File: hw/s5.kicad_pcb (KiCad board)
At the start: 2 copper layers, 110 x 53 mm, 220 parts, among them J1 Conn_01x02, J12 USB_C_Receptacle, J2 RJ45, J3 RJ45, J4 RJ45, J5 RJ45, J6 RJ45, J7 Conn_01x03, Q1 NMOS, Q2 NMOS, Q3 NMOS, Q4 NMOS, Q5 NMOS, SW1 SW_Push, SW2 SW_Push, T1 GBE_XFMR, T2 GBE_XFMR, T3 GBE_XFMR, T4 GBE_XFMR, T5 GBE_XFMR, U1 KSZ9477S, U10 TPS3823, U11 TLV62569, U12 AP2112K-1.8, U13 TPS23861, U2 AMS1117-3.3, U3 AP2112K-2.5, U4 AP2112K-1.2, U6 TPS54560, U7 T113-S3, U8 W25Q128JVSIQ, U9 TPS23861, Y1 25MHz, Y2 24MHz, Y3 32.768kHz

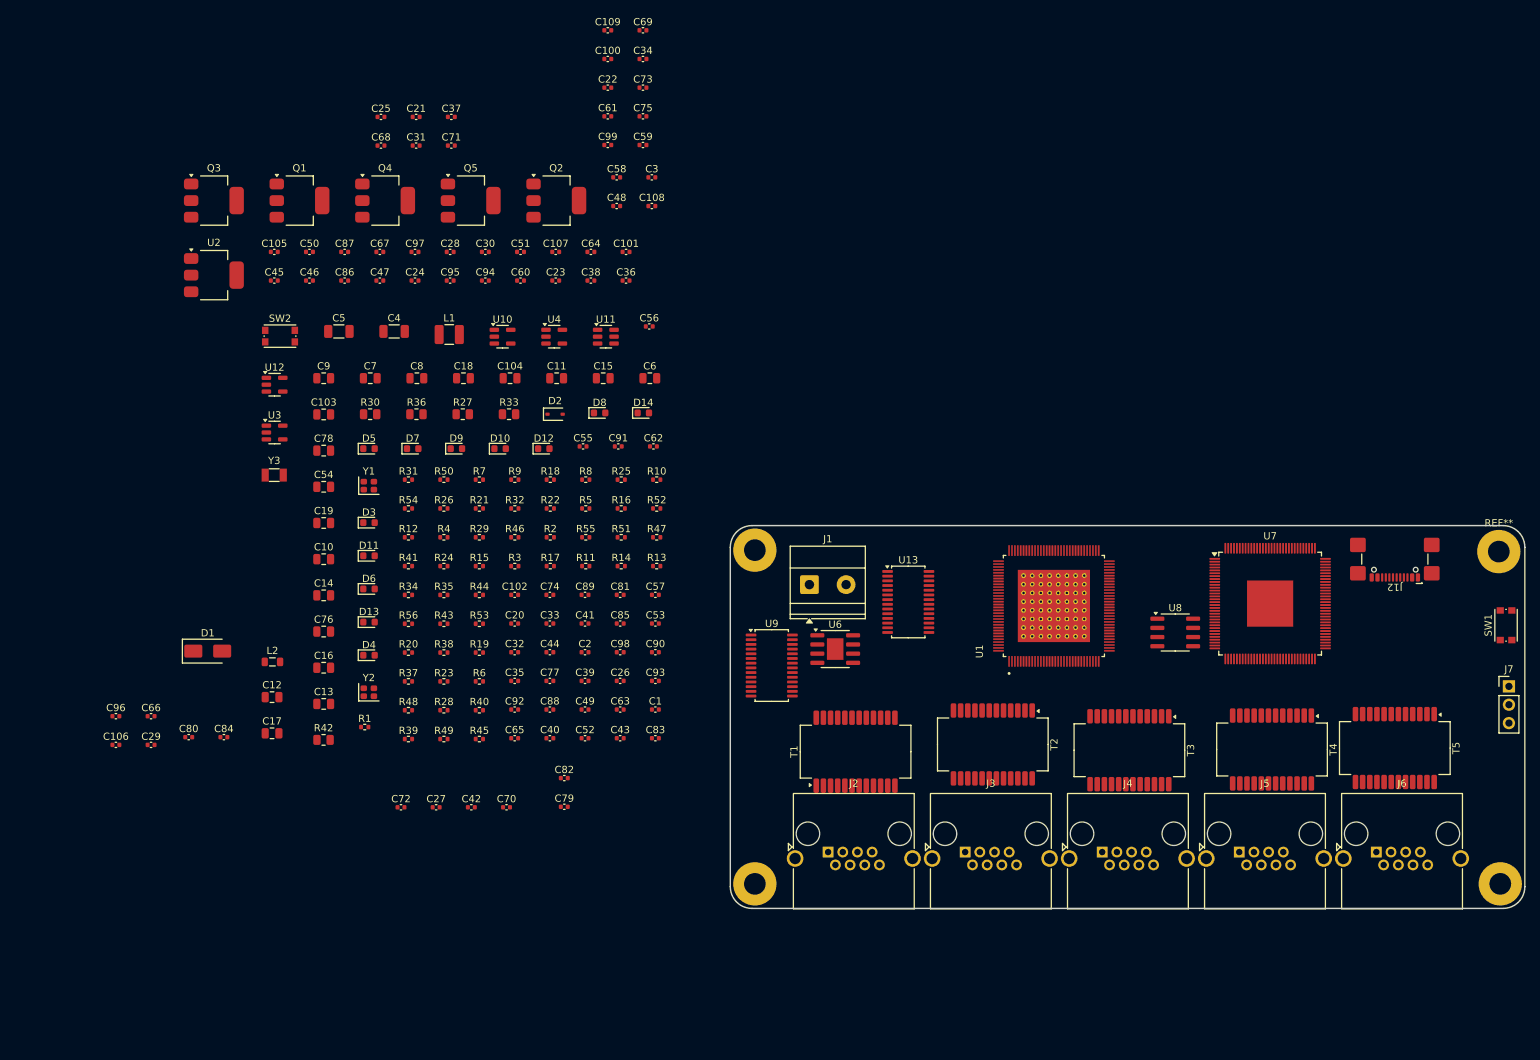
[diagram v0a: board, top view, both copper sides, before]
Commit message: Barrel jack, drop BOOT button, 256MB NAND flash, net classes
- Power input: terminal block -> 5.5/2.5mm barrel jack (48V Meanwell)
- Remove SW1 (FEL/boot button), keep only reset (SW2)
- Flash: W25Q128 SPI NOR (16MB) -> W25N02 SPI NAND (256MB) for
  full einheit stack + web UI
- Net classes: MDI (0.12mm/0.15mm clearance), RGMII, POWER with
  auto-assignment patterns; via sizes 0.3/0.45/0.6/0.8mm
- Track widths reduced to 0.12mm for KSZ9477 QFP escape (0.4mm pitch)
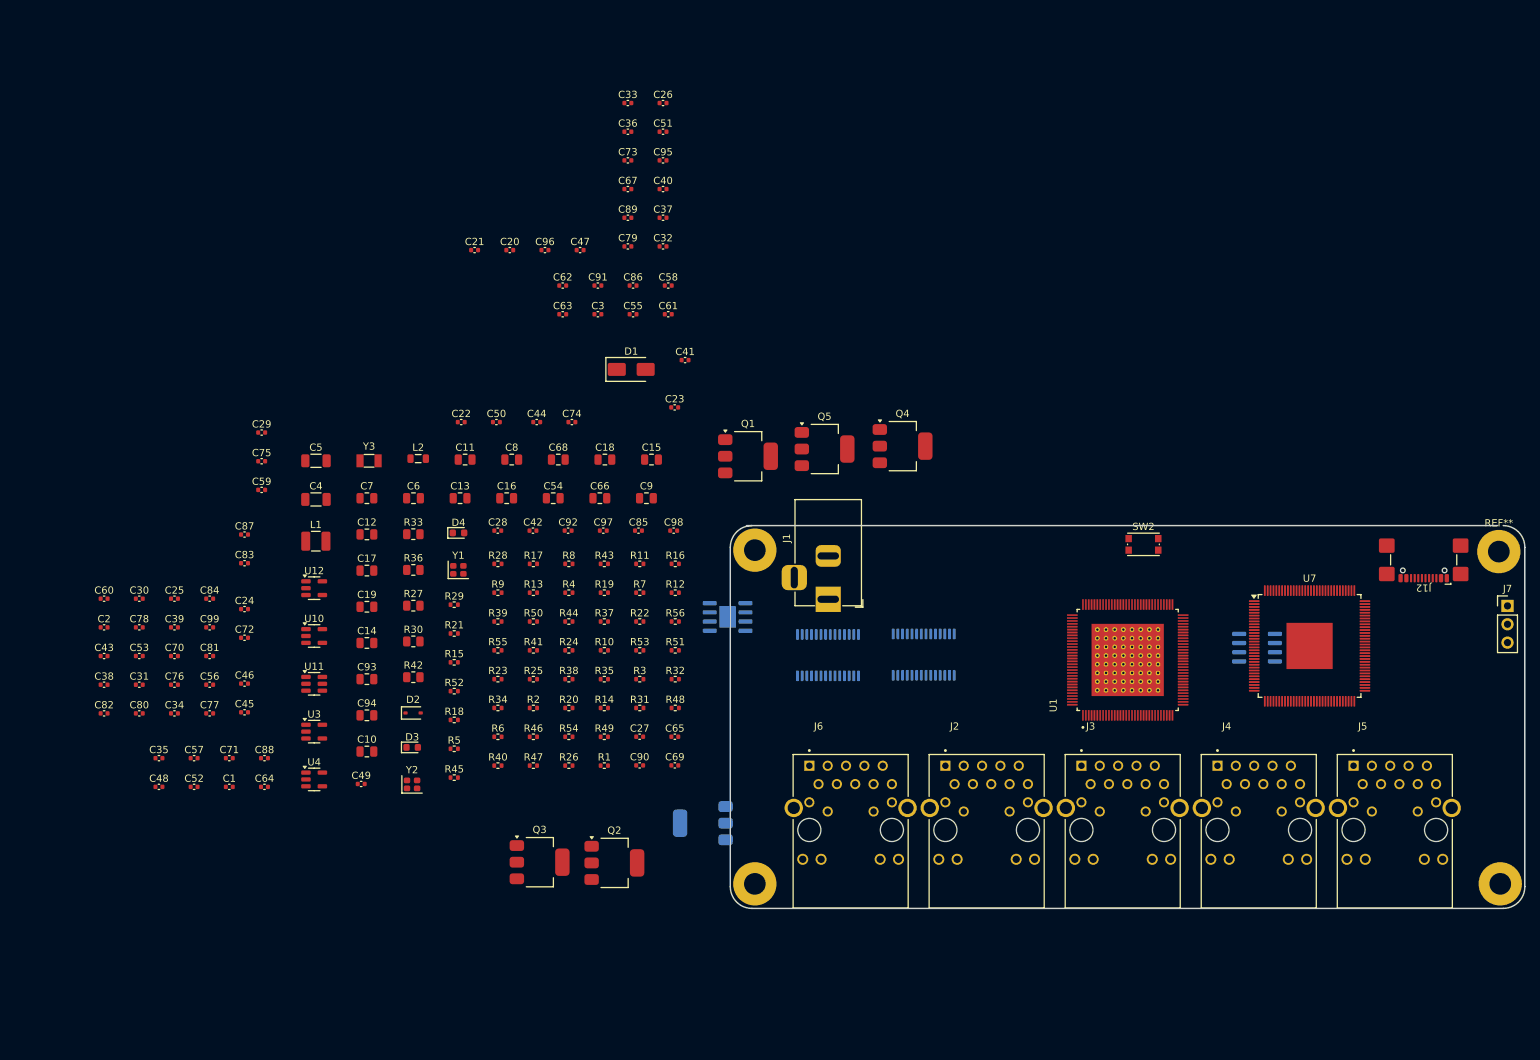
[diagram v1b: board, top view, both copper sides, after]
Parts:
- removed C100, C101, C102, C107, C108, C109: 100nF, Capacitor_SMD:C_0402_1005Metric
- removed C103, C104: 10uF, Capacitor_SMD:C_0805_2012Metric
- removed C105, C106: 18pF, Capacitor_SMD:C_0402_1005Metric
- removed D10, D11, D12, D13, D14, D5, D6, D7, D8, D9: LED, LED_SMD:LED_0603_1608Metric
- removed SW1: SW_Push, Button_Switch_SMD:SW_Push_1P1T_NO_CK_KMR2
- removed T1, T2, T3, T4, T5: GBE_XFMR, Transformer_SMD:Transformer_Ethernet_YDS_30F-51NL_SO-24_7.1x15.1mm
- C66, C68: footprint Capacitor_SMD:C_0402_1005Metric -> Capacitor_SMD:C_0805_2012Metric
- C69, C70: value 100nF -> 1uF
- C76, C78: footprint Capacitor_SMD:C_0805_2012Metric -> Capacitor_SMD:C_0402_1005Metric
- C79, C80: value 1uF -> 100nF
- C93, C94: value 100nF -> 10uF; footprint Capacitor_SMD:C_0402_1005Metric -> Capacitor_SMD:C_0805_2012Metric
- C95, C96: value 100nF -> 18pF
- J1: value Conn_01x02 -> BarrelJack; footprint TerminalBlock_Phoenix:TerminalBlock_Phoenix_MKDS-1,5-2-5.08_1x02_P5.08mm_Horizontal -> Connector_BarrelJack:BarrelJack_Horizontal
- J2, J3, J4, J5, J6: value RJ45 -> LPJG0926HENL; footprint Connector_RJ:RJ45_Amphenol_RJHSE5380 -> connectors:LPJG0926HENL
- R15, R16, R17, R18, R19, R20, R21, R22, R23, R24: value 270 -> 150
- U13, U2, U6, U8, U9: moved to B.Cu
- moved SW2 123.0 mm to (162.2, 87.6)
- moved C34 111.4 mm to (28.1, 111.0)
- moved C48 102.4 mm to (25.9, 121.2)
- moved Q3 102.1 mm to (78.6, 131.6)
- moved C69 101.9 mm to (97.3, 118.2)
- moved U2 101.7 mm to (101.2, 126.2), turned to 180 degrees
- moved Q2 92.0 mm to (89.0, 131.7)
- moved C71 90.2 mm to (35.6, 117.2)
- moved C96 87.7 mm to (79.3, 46.9)
- moved C38 87.6 mm to (18.3, 107.0)
- moved C64 86.8 mm to (40.5, 121.2)
- moved C99 86.6 mm to (32.9, 99.1)
- moved C31 83.9 mm to (23.2, 107.0)
- moved C26 80.2 mm to (95.7, 26.5)
- moved Q4 79.3 mm to (128.8, 74.0)
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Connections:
- C55 pad 1: P1_A_CT -> P1_CT1
- C56 pad 1: P1_B_CT -> P1_CT2
- C57 pad 1: P1_C_CT -> P2_CT1
- C58 pad 1: P1_D_CT -> P2_CT2
- C59 pad 1: P2_A_CT -> P3_CT1
- C60 pad 1: P2_B_CT -> P3_CT2
- C61 pad 1: P2_C_CT -> P4_CT1
- C62 pad 1: P2_D_CT -> P4_CT2
- C63 pad 1: P3_A_CT -> P5_CT1
- C64 pad 1: P3_B_CT -> P5_CT2
- C65 pad 1: P3_C_CT -> VDD_3V3
- C66 pad 1: P3_D_CT -> VIN_48V
- C67 pad 1: P4_A_CT -> VDD_3V3
- C68 pad 1: P4_B_CT -> VIN_48V
- C69 pad 1: P4_C_CT -> N$11
- C70 pad 1: P4_D_CT -> N$12
- C71 pad 1: P5_A_CT -> VDD_3V3
- C72 pad 1: P5_B_CT -> VDD_3V3
- C73 pad 1: P5_C_CT -> VDD_3V3
- C74 pad 1: P5_D_CT -> VDD_3V3
- C76 pad 1: VIN_48V -> VDD_3V3
- C78 pad 1: VIN_48V -> VDD_3V3
- C79 pad 1: N$1 -> VDD_3V3
- C80 pad 1: N$2 -> VDD_3V3
- C83 pad 1: VDD_3V3 -> VDD_CORE
- C84 pad 1: VDD_3V3 -> VDD_CORE
- C85 pad 1: VDD_3V3 -> VDD_CORE
- C86 pad 1: VDD_3V3 -> VDD_CORE
- C87 pad 1: VDD_3V3 -> VDD_CORE
- C88 pad 1: VDD_3V3 -> VDD_CORE
- C89 pad 1: VDD_3V3 -> VDD_1V8
- C90 pad 1: VDD_3V3 -> VDD_1V8
- C91 pad 1: VDD_3V3 -> VDD_1V8
- C92 pad 1: VDD_3V3 -> VDD_1V8
- C94 pad 1: VDD_CORE -> VDD_3V3
- C95 pad 1: VDD_CORE -> T113_DXIN
- C96 pad 1: VDD_CORE -> T113_DXOUT
- C97 pad 1: VDD_CORE -> SOC_RESET_N
- C98 pad 1: VDD_CORE -> VDD_3V3
- C99 pad 1: VDD_1V8 -> VDD_3V3
- D3 pad 1: ETH_LED1_0_A -> LED_PWR_A
- D3 pad 2: ETH_LED1_0 -> GND
- D4 pad 1: ETH_LED1_1_A -> LED_STA_A
- D4 pad 2: ETH_LED1_1 -> LED_STATUS
- J2 pad 1: P1_LINE_1 -> P1_AP
- J2 pad 2: P1_LINE_2 -> P1_AN
- J2 pad 3: P1_LINE_3 -> P1_BP
- J2 pad 4: P1_LINE_4 -> P1_CT1
- J2 pad 5: P1_LINE_5 -> P1_CT2
- J2 pad 6: P1_LINE_6 -> P1_BN
- J2 pad 7: P1_LINE_7 -> P1_CP
- J2 pad 8: P1_LINE_8 -> P1_CN
- J3 pad 1: P2_LINE_1 -> P2_AP
- J3 pad 2: P2_LINE_2 -> P2_AN
- J3 pad 3: P2_LINE_3 -> P2_BP
- J3 pad 4: P2_LINE_4 -> P2_CT1
- J3 pad 5: P2_LINE_5 -> P2_CT2
- J3 pad 6: P2_LINE_6 -> P2_BN
- J3 pad 7: P2_LINE_7 -> P2_CP
- J3 pad 8: P2_LINE_8 -> P2_CN
- J4 pad 1: P3_LINE_1 -> P3_AP
- J4 pad 2: P3_LINE_2 -> P3_AN
- J4 pad 3: P3_LINE_3 -> P3_BP
- J4 pad 4: P3_LINE_4 -> P3_CT1
- J4 pad 5: P3_LINE_5 -> P3_CT2
- J4 pad 6: P3_LINE_6 -> P3_BN
- J4 pad 7: P3_LINE_7 -> P3_CP
- J4 pad 8: P3_LINE_8 -> P3_CN
- J5 pad 1: P4_LINE_1 -> P4_AP
- J5 pad 2: P4_LINE_2 -> P4_AN
- J5 pad 3: P4_LINE_3 -> P4_BP
- J5 pad 4: P4_LINE_4 -> P4_CT1
- J5 pad 5: P4_LINE_5 -> P4_CT2
- J5 pad 6: P4_LINE_6 -> P4_BN
- J5 pad 7: P4_LINE_7 -> P4_CP
- J5 pad 8: P4_LINE_8 -> P4_CN
- J6 pad 1: P5_LINE_1 -> P5_AP
- J6 pad 2: P5_LINE_2 -> P5_AN
- J6 pad 3: P5_LINE_3 -> P5_BP
- J6 pad 4: P5_LINE_4 -> P5_CT1
- J6 pad 5: P5_LINE_5 -> P5_CT2
- J6 pad 6: P5_LINE_6 -> P5_BN
- J6 pad 7: P5_LINE_7 -> P5_CP
- J6 pad 8: P5_LINE_8 -> P5_CN
- R15 pad 2: ETH_LED1_0_A -> N$1
- R16 pad 2: ETH_LED1_1_A -> N$2
- R17 pad 2: ETH_LED2_0_A -> N$3
- R18 pad 2: ETH_LED2_1_A -> N$4
- R19 pad 2: ETH_LED3_0_A -> N$5
- R20 pad 2: ETH_LED3_1_A -> N$6
- R21 pad 2: ETH_LED4_0_A -> N$7
- R22 pad 2: ETH_LED4_1_A -> N$8
- R23 pad 2: ETH_LED5_0_A -> N$9
- R24 pad 2: ETH_LED5_1_A -> N$10
- U1 pad 102: ETH_LED5_0 -> P5_GRN
- U1 pad 103: ETH_LED5_1 -> P5_YEL
- U1 pad 105: ETH_LED1_0 -> P1_GRN
- U1 pad 106: ETH_LED1_1 -> P1_YEL
- U1 pad 85: ETH_LED4_0 -> P4_GRN
- U1 pad 86: ETH_LED4_1 -> P4_YEL
- U1 pad 88: ETH_LED3_0 -> P3_GRN
- U1 pad 89: ETH_LED3_1 -> P3_YEL
- U1 pad 91: ETH_LED2_0 -> P2_GRN
- U1 pad 92: ETH_LED2_1 -> P2_YEL
- U7 pad 28: N$1 -> N$11
- U7 pad 30: N$2 -> N$12
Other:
- outline, holes or cut-outs redrawn

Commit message: Add S5 switch adapter with PoE control, fix USB-C footprint
Software:
- Scaffold einheit-cli switch adapter from s100, ported to s5
  namespace with KSZ9477 DSA + TPS23861 PoE I2C control.
- Commands: show interfaces/counters/vlans/mac-table/poe/system,
  set poe enable/disable/reset, set hostname/ip/dns/ntp/user,
  shell, ping, traceroute, reboot.
- poe.cc: TPS23861 I2C driver skeleton — U9 (0x20, ports 1-4),
  U13 (0x28, port 5). Register map TODOs for voltage/current
  scaling.
- Builds and runs on host (0 errors, PoE gracefully degrades
  when I2C bus unavailable).

Hardware:
- Fix USB-C footprint: remove overlapping pads (A1/B12, A4/B9,
  A9/B4, A12/B1 merged), local copy in connectors.pretty.
- Named all anonymous nets (N$2-N$13 -> proper signal names).
- Added empty.kicad_wks page template.
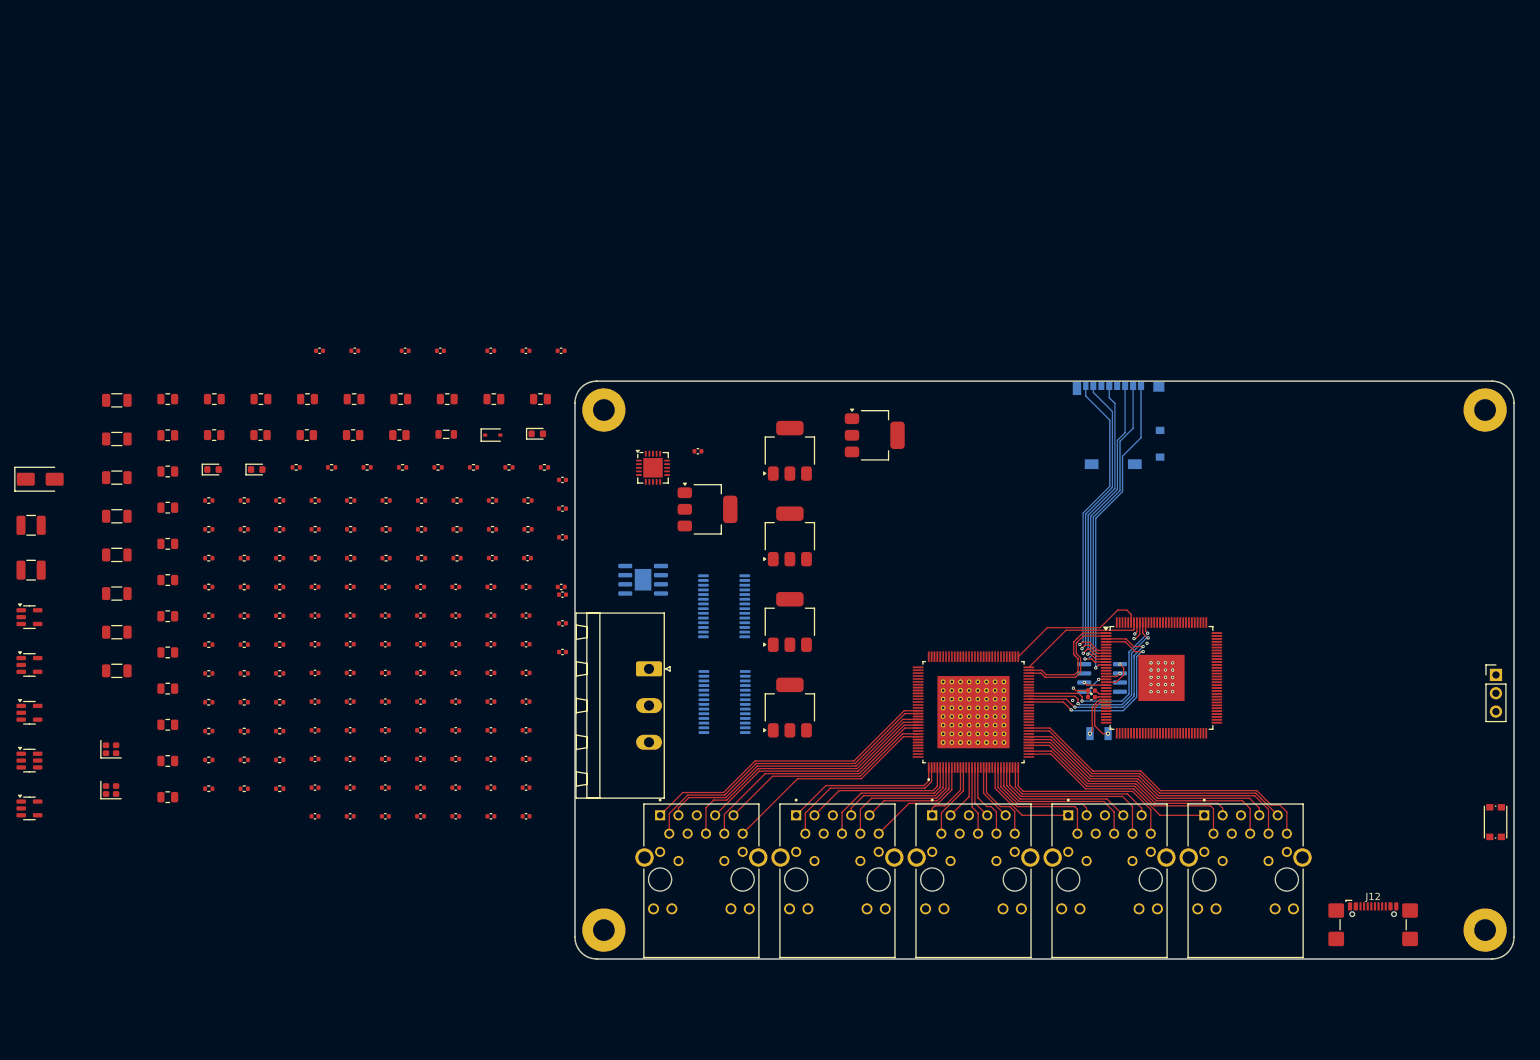
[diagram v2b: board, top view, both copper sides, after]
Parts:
- removed ? (x3): , 
- removed the REF** at (211.4, 88.6)
- added C100: 100nF, Capacitor_SMD:C_0402_1005Metric, F.Cu at (71.9, 113.3)
- added C101: 100nF, Capacitor_SMD:C_0402_1005Metric, F.Cu at (71.9, 109.4)
- added C102: 100nF, Capacitor_SMD:C_0402_1005Metric, F.Cu at (57.2, 105.4)
- added C103: 10uF, Capacitor_SMD:C_0805_2012Metric, F.Cu at (72.3, 67.5)
- added C104: 10uF, Capacitor_SMD:C_0805_2012Metric, F.Cu at (27.1, 107.6)
- added C105: 18pF, Capacitor_SMD:C_0402_1005Metric, F.Cu at (155.0, 108.8)
- added C106: 18pF, Capacitor_SMD:C_0402_1005Metric, F.Cu at (155.0, 107.8)
- added C107: 100nF, Capacitor_SMD:C_0402_1005Metric, F.Cu at (81.6, 60.8)
- added C108: 100nF, Capacitor_SMD:C_0402_1005Metric, F.Cu at (76.7, 109.4)
- added C109: 100nF, Capacitor_SMD:C_0402_1005Metric, F.Cu at (67.0, 117.3)
- added C110: 100nF, Capacitor_SMD:C_0402_1005Metric, F.Cu at (100.5, 74.7)
- added D5: LED, LED_SMD:LED_0603_1608Metric, F.Cu at (78.3, 72.3)
- added J8: microSD, Connector_Card:microSD_HC_Molex_104031-0811, B.Cu at (158.8, 71.1)
- added L3: 1uH, Inductor_SMD:L_0805_2012Metric, F.Cu at (65.7, 72.4)
- added R57: 10k, Resistor_SMD:R_0402_1005Metric, F.Cu at (37.7, 105.5)
- added R58: 10k, Resistor_SMD:R_0402_1005Metric, F.Cu at (44.9, 76.9)
- added R59: 27, Resistor_SMD:R_0402_1005Metric, F.Cu at (42.6, 97.5)
- added R60: 27, Resistor_SMD:R_0402_1005Metric, F.Cu at (72.1, 85.5)
- added R61: 5.1k, Resistor_SMD:R_0402_1005Metric, F.Cu at (32.8, 101.5)
- added R62: 5.1k, Resistor_SMD:R_0402_1005Metric, F.Cu at (77.0, 81.5)
- added R63: 270, Resistor_SMD:R_0402_1005Metric, F.Cu at (32.8, 113.5)
- added R64: 270, Resistor_SMD:R_0402_1005Metric, F.Cu at (42.6, 89.5)
- added R65: 270, Resistor_SMD:R_0402_1005Metric, F.Cu at (74.4, 76.9)
- added REF**: MountingHole_3mm_Pad, MountingHole:MountingHole_3mm_Pad, F.Cu at (209.5, 69.0)
- added REF**: MountingHole_3mm_Pad, MountingHole:MountingHole_3mm_Pad, F.Cu at (87.5, 141.0)
- added REF**: MountingHole_3mm_Pad, MountingHole:MountingHole_3mm_Pad, F.Cu at (209.5, 141.0)
- added REF**: MountingHole_3mm_Pad, MountingHole:MountingHole_3mm_Pad, F.Cu at (87.5, 69.0)
- added U14: LM5122, Package_DFN_QFN:QFN-20-1EP_4x4mm_P0.5mm_EP2.7x2.7mm, F.Cu at (94.3, 77.0)
- C1: value 100nF -> 100uF; footprint Capacitor_SMD:C_0402_1005Metric -> Capacitor_SMD:C_1206_3216Metric
- C10, C8, C9: footprint Capacitor_SMD:C_0805_2012Metric -> Capacitor_SMD:C_1206_3216Metric
- C11, C12, C54, C93, C94: value 10uF -> 100nF; footprint Capacitor_SMD:C_0805_2012Metric -> Capacitor_SMD:C_0402_1005Metric
- C13: value 10uF -> 15nF; footprint Capacitor_SMD:C_0805_2012Metric -> Capacitor_SMD:C_0402_1005Metric
- C14, C15: value 10uF -> 2.2uF; footprint Capacitor_SMD:C_0805_2012Metric -> Capacitor_SMD:C_1206_3216Metric
- C16, C17, C19: value 10uF -> 22uF
- C2: value 100nF -> 4.7uF; footprint Capacitor_SMD:C_0402_1005Metric -> Capacitor_SMD:C_0805_2012Metric
- C20: value 100nF -> 22uF; footprint Capacitor_SMD:C_0402_1005Metric -> Capacitor_SMD:C_0805_2012Metric
- C21, C22, C23, C24, C25, C26, C27, C28, C29, C64: value 100nF -> 10uF; footprint Capacitor_SMD:C_0402_1005Metric -> Capacitor_SMD:C_0805_2012Metric
- C3: value 15nF -> 100nF
- C4: value 2.2uF -> 100nF; footprint Capacitor_SMD:C_1206_3216Metric -> Capacitor_SMD:C_0402_1005Metric
- C5: value 2.2uF -> 10nF; footprint Capacitor_SMD:C_1206_3216Metric -> Capacitor_SMD:C_0402_1005Metric
- C52, C53: value 15pF -> 100nF
- C6, C7: value 22uF -> 10uF; footprint Capacitor_SMD:C_0805_2012Metric -> Capacitor_SMD:C_1206_3216Metric
- C62, C63: value 100nF -> 15pF
- C66, C68: footprint Capacitor_SMD:C_0805_2012Metric -> Capacitor_SMD:C_0402_1005Metric
- C69, C70: value 1uF -> 100nF
- C76, C78: footprint Capacitor_SMD:C_0402_1005Metric -> Capacitor_SMD:C_0805_2012Metric
- C79, C80: value 100nF -> 1uF
- C95, C96: value 18pF -> 100nF
- J1: value BarrelJack -> Conn_01x03; footprint Connector_BarrelJack:BarrelJack_Horizontal -> Connector_Phoenix_MSTB:PhoenixContact_MSTB_2,5_3-GF-5,08_1x03_P5.08mm_Horizontal_ThreadedFlange
- J12: footprint Connector_USB:USB_C_Receptacle_GCT_USB4110 -> connectors:USB_C_GCT_USB4110
- L1: value 33uH -> 10uH
- L2: value 1uH -> 33uH; footprint Inductor_SMD:L_0805_2012Metric -> Inductor_SMD:L_1210_3225Metric
- R1: value 24.9k -> 150k
- R10: value 4.7k -> 52.3k
- R12: value 10k -> 50k
- R13, R8: value 10k -> 100k
- R14: value 1k -> 6.04k
- R15: value 150 -> 191
- R16, R19, R20, R21: value 150 -> 10k
- R17, R18: value 150 -> 4.7k
- R2: value 52.3k -> 100k
- R22: value 150 -> 1k
- R25: value 10k -> 150
- R26, R29, R32: value 47 -> 150
- R27, R30: value 0.25 -> 150; footprint Resistor_SMD:R_0805_2012Metric -> Resistor_SMD:R_0402_1005Metric
- R28, R31: value 22 -> 150
- R3: value 10k -> 6.8k
- R33: value 0.25 -> 10k; footprint Resistor_SMD:R_0805_2012Metric -> Resistor_SMD:R_0402_1005Metric
- R34, R37, R43: value 22 -> 47
- R35, R41: value 47 -> 0.25; footprint Resistor_SMD:R_0402_1005Metric -> Resistor_SMD:R_0805_2012Metric
- R36, R42: value 0.25 -> 22; footprint Resistor_SMD:R_0805_2012Metric -> Resistor_SMD:R_0402_1005Metric
- R38, R44: value 22 -> 0.25; footprint Resistor_SMD:R_0402_1005Metric -> Resistor_SMD:R_0805_2012Metric
- R4: value 50k -> 33k
- R40, R49: value 10k -> 47
- R45, R46: value 4.7k -> 22
- R47: value 240 -> 22
- R5: value 100k -> 383k
- R50: value 10k -> 0.25; footprint Resistor_SMD:R_0402_1005Metric -> Resistor_SMD:R_0805_2012Metric
- R51, R52: value 27 -> 22
- R53, R54: value 5.1k -> 4.7k
- R55: value 270 -> 240
- R56: value 270 -> 10k
- R6: value 6.04k -> 10k
- R7: value 191 -> 10k
- R9: value 4.7k -> 24.9k
- U2: moved to F.Cu
- U8: value W25Q128JVSIQ -> W25N02JWZEIF
- Y3: moved to B.Cu
- moved C26 114.0 mm to (27.1, 117.6)
- moved Y3 107.9 mm to (156.1, 113.8)
- moved C33 95.8 mm to (76.7, 121.3)
- moved C21 86.8 mm to (27.1, 122.6)
- moved D1 83.2 mm to (9.46, 78.6)
- moved C55 79.8 mm to (52.4, 125.2)
- moved C40 77.3 mm to (76.7, 113.3)
- moved C79 76.5 mm to (62.1, 117.3)
- moved C91 76.3 mm to (47.5, 117.3)
- moved C36 76.2 mm to (76.7, 105.4)
- moved C51 74.9 mm to (71.9, 101.4)
- moved C95 74.9 mm to (71.9, 105.4)
- moved C15 74.4 mm to (20.1, 83.7)
- moved C23 74.1 mm to (27.1, 92.5)
- moved C9 73.7 mm to (20.1, 89.1)
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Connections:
- C1 pad 1: BOOT -> VIN_24V
- C1 pad 2: SW_NODE -> GND
- C10 pad 1: VDD_CORE -> VIN_24V
- C11 pad 1: VDD_1V8 -> BOOT
- C11 pad 2: GND -> SW_NODE
- C12 pad 1: VDD_1V8 -> SS_TR
- C13 pad 1: VIN_48V -> COMP_MID
- C14 pad 1: VDD_5V -> VIN_24V
- C15 pad 1: VDD_3V3 -> VIN_24V
- C16 pad 1: VDD_2V5 -> VDD_5V
- C17 pad 1: VDD_1V2 -> VDD_5V
- C18 pad 1: VDD_CORE -> VDD_5V
- C19 pad 1: VDD_1V8 -> VDD_CORE
- C2 pad 1: SS_TR -> BOOST_VCC
- C20 pad 1: VDD_2V5 -> VDD_CORE
- C21 pad 1: VDD_2V5 -> VDD_1V8
- C22 pad 1: VDD_2V5 -> VDD_1V8
- C23 pad 1: VDD_2V5 -> VIN_24V
- C24 pad 1: VDD_2V5 -> VDD_5V
- C25 pad 1: VDD_2V5 -> VDD_3V3
- C27 pad 1: VDD_2V5 -> VDD_1V2
- C28 pad 1: VDD_2V5 -> VDD_CORE
- C29 pad 1: VDD_1V2 -> VDD_1V8
- C3 pad 1: COMP_MID -> BST_BOOST
- C3 pad 2: GND -> BOOST_SW
- C30 pad 1: VDD_1V2 -> VDD_2V5
- C31 pad 1: VDD_1V2 -> VDD_2V5
- C32 pad 1: VDD_1V2 -> VDD_2V5
- C33 pad 1: VDD_1V2 -> VDD_2V5
- C34 pad 1: VDD_1V2 -> VDD_2V5
- C35 pad 1: VDD_1V2 -> VDD_2V5
- C36 pad 1: VDD_1V2 -> VDD_2V5
- C37 pad 1: VDD_1V2 -> VDD_2V5
- C38 pad 1: VDD_1V2 -> VDD_2V5
- C4 pad 1: VIN_48V -> BOOST_SS
- C49 pad 1: VDD_3V3 -> VDD_1V2
- C5 pad 1: VIN_48V -> BOOST_COMP_MID
- C50 pad 1: VDD_3V3 -> VDD_1V2
- C51 pad 1: VDD_3V3 -> VDD_1V2
- C52 pad 1: KSZ_XI -> VDD_1V2
- C53 pad 1: KSZ_XO -> VDD_1V2
- C54 pad 1: KSZ_RESET_N -> VDD_1V2
- C55 pad 1: P1_CT1 -> VDD_1V2
- C56 pad 1: P1_CT2 -> VDD_1V2
- C57 pad 1: P2_CT1 -> VDD_1V2
- C58 pad 1: P2_CT2 -> VDD_1V2
- C59 pad 1: P3_CT1 -> VDD_3V3
- C6 pad 1: VDD_5V -> VBUS_48V
- C60 pad 1: P3_CT2 -> VDD_3V3
- C61 pad 1: P4_CT1 -> VDD_3V3
- C62 pad 1: P4_CT2 -> KSZ_XI
- C63 pad 1: P5_CT1 -> KSZ_XO
- C64 pad 1: P5_CT2 -> KSZ_RESET_N
- C65 pad 1: VDD_3V3 -> P1_CT1
- C66 pad 1: VIN_48V -> P1_CT2
- C67 pad 1: VDD_3V3 -> P2_CT1
- C68 pad 1: VIN_48V -> P2_CT2
- C69 pad 1: N$11 -> P3_CT1
- C7 pad 1: VDD_5V -> VBUS_48V
- C70 pad 1: N$12 -> P3_CT2
- C71 pad 1: VDD_3V3 -> P4_CT1
- C72 pad 1: VDD_3V3 -> P4_CT2
- C73 pad 1: VDD_3V3 -> P5_CT1
- C74 pad 1: VDD_3V3 -> P5_CT2
- C76 pad 1: VDD_3V3 -> VBUS_48V
- C78 pad 1: VDD_3V3 -> VBUS_48V
- C79 pad 1: VDD_3V3 -> N$12
- C8 pad 1: VDD_5V -> VBUS_48V
- C80 pad 1: VDD_3V3 -> N$13
- C83 pad 1: VDD_CORE -> VDD_3V3
- C84 pad 1: VDD_CORE -> VDD_3V3
- C85 pad 1: VDD_CORE -> VDD_3V3
- C86 pad 1: VDD_CORE -> VDD_3V3
- C87 pad 1: VDD_CORE -> VDD_3V3
- C88 pad 1: VDD_CORE -> VDD_3V3
- C89 pad 1: VDD_1V8 -> VDD_3V3
- C9 pad 1: VDD_CORE -> VIN_24V
- C90 pad 1: VDD_1V8 -> VDD_3V3
- C91 pad 1: VDD_1V8 -> VDD_3V3
- C92 pad 1: VDD_1V8 -> VDD_3V3
- C94 pad 1: VDD_3V3 -> VDD_CORE
- C95 pad 1: T113_DXIN -> VDD_CORE
- C96 pad 1: T113_DXOUT -> VDD_CORE
- C97 pad 1: SOC_RESET_N -> VDD_CORE
- C98 pad 1: VDD_3V3 -> VDD_CORE
- C99 pad 1: VDD_3V3 -> VDD_1V8
- J1 pad 1: VIN_48V -> VIN_24V
- J1 pad 3: GND -> PE
- J12 pad A12: (no net) -> GND
- J12 pad A4: (no net) -> USB_VBUS
- J12 pad A9: (no net) -> USB_VBUS
- J2 pad 15: N$1 -> N$2
- J2 pad 17: N$2 -> N$3
- J3 pad 15: N$3 -> N$4
- J3 pad 17: N$4 -> N$5
- J4 pad 15: N$5 -> N$6
- J4 pad 17: N$6 -> N$7
- J5 pad 15: N$7 -> N$8
- J5 pad 17: N$8 -> N$9
- J6 pad 15: N$9 -> N$10
- J6 pad 17: N$10 -> N$11
- L1 pad 1: SW_NODE -> VIN_24V
- L1 pad 2: VDD_5V -> BOOST_SW
- L2 pad 1: CORE_SW -> SW_NODE
- L2 pad 2: VDD_CORE -> VDD_5V
- Q1 pad 2: VIN_48V -> VBUS_48V
- Q2 pad 2: VIN_48V -> VBUS_48V
- Q3 pad 2: VIN_48V -> VBUS_48V
- Q4 pad 2: VIN_48V -> VBUS_48V
- Q5 pad 2: VIN_48V -> VBUS_48V
- R1 pad 1: COMP -> BOOST_RT
- R1 pad 2: COMP_MID -> GND
- R10 pad 1: VDD_3V3 -> VDD_5V
- R10 pad 2: SPI_CS_N -> FB_5V
- R11 pad 1: VDD_3V3 -> FB_5V
- R11 pad 2: INTRP_N -> GND
- R12 pad 1: VDD_3V3 -> VDD_CORE
- R12 pad 2: PME_N -> FB_0V9
- R13 pad 1: VDD_3V3 -> FB_0V9
- R13 pad 2: SYNCLKO -> GND
- R14 pad 1: IBA -> KSZ_ISET
- R15 pad 1: VDD_3V3 -> KSZ_S_REXT
- R15 pad 2: N$1 -> GND
- R16 pad 2: N$2 -> KSZ_RESET_N
- R17 pad 2: N$3 -> SPI_MOSI
- R18 pad 2: N$4 -> SPI_CS_N
- R19 pad 2: N$5 -> INTRP_N
- R2 pad 1: VDD_5V -> VIN_24V
- R2 pad 2: FB_5V -> BOOST_UVLO
- R20 pad 2: N$6 -> PME_N
- R21 pad 2: N$7 -> SYNCLKO
- R22 pad 1: VDD_3V3 -> IBA
- R22 pad 2: N$8 -> GND
- R23 pad 2: N$9 -> N$2
- R24 pad 2: N$10 -> N$3
- R25 pad 2: U9_RESET -> N$4
- R26 pad 1: VIN_48V -> VDD_3V3
- R26 pad 2: U9_DRAIN16 -> N$5
- R27 pad 1: U9_SRC15 -> VDD_3V3
- R27 pad 2: POE_VP_1 -> N$6
- R28 pad 1: U9_SRC15 -> VDD_3V3
- R28 pad 2: U9_SEN15 -> N$7
- R29 pad 1: VIN_48V -> VDD_3V3
- R29 pad 2: U9_DRAIN20 -> N$8
- R3 pad 1: FB_5V -> BOOST_UVLO
- R30 pad 1: U9_SRC19 -> VDD_3V3
- R30 pad 2: POE_VP_2 -> N$9
- R31 pad 1: U9_SRC19 -> VDD_3V3
- R31 pad 2: U9_SEN19 -> N$10
- R32 pad 1: VIN_48V -> VDD_3V3
- R32 pad 2: U9_DRAIN9 -> N$11
- R33 pad 1: U9_SRC8 -> VDD_3V3
- R33 pad 2: POE_VP_3 -> U9_RESET
- R34 pad 1: U9_SRC8 -> VBUS_48V
- R34 pad 2: U9_SEN8 -> U9_DRAIN16
- R35 pad 1: VIN_48V -> U9_SRC15
- R35 pad 2: U9_DRAIN13 -> POE_VP_1
- R36 pad 1: U9_SRC12 -> U9_SRC15
- R36 pad 2: POE_VP_4 -> U9_SEN15
- R37 pad 1: U9_SRC12 -> VBUS_48V
- R37 pad 2: U9_SEN12 -> U9_DRAIN20
- R38 pad 1: U9_KSENSA -> U9_SRC19
- R38 pad 2: GND -> POE_VP_2
- R39 pad 1: U9_KSENSB -> U9_SRC19
- R39 pad 2: GND -> U9_SEN19
- R4 pad 1: VDD_CORE -> BOOST_ILIM
- R4 pad 2: FB_0V9 -> GND
- R40 pad 1: VDD_3V3 -> VBUS_48V
- R40 pad 2: U13_RESET -> U9_DRAIN9
- R41 pad 1: VIN_48V -> U9_SRC8
- R41 pad 2: U13_DRAIN16 -> POE_VP_3
- R42 pad 1: U13_SRC15 -> U9_SRC8
- R42 pad 2: POE_VP_5 -> U9_SEN8
- R43 pad 1: U13_SRC15 -> VBUS_48V
- R43 pad 2: U13_SEN15 -> U9_DRAIN13
- R44 pad 1: U13_KSENSA -> U9_SRC12
- R44 pad 2: GND -> POE_VP_4
- R45 pad 1: VDD_3V3 -> U9_SRC12
- R45 pad 2: PSE_I2C_SDA -> U9_SEN12
- R46 pad 1: VDD_3V3 -> U9_KSENSA
- R46 pad 2: PSE_I2C_SCL -> GND
- R47 pad 1: T113_DZQ -> U9_KSENSB
- R48 pad 2: SOC_RESET_N -> U13_RESET
- R49 pad 1: VDD_3V3 -> VBUS_48V
- R49 pad 2: FLASH_WP -> U13_DRAIN16
- R5 pad 1: FB_0V9 -> VBUS_48V
- R5 pad 2: GND -> BOOST_FB
- R50 pad 1: VDD_3V3 -> U13_SRC15
- R50 pad 2: FLASH_HOLD -> POE_VP_5
- R51 pad 1: USB_DP -> U13_SRC15
- R51 pad 2: USB_CONN_DP -> U13_SEN15
- R52 pad 1: USB_DM -> U13_KSENSA
- R52 pad 2: USB_CONN_DM -> GND
- R53 pad 1: USB_CC1 -> VDD_3V3
- R53 pad 2: GND -> PSE_I2C_SDA
- R54 pad 1: USB_CC2 -> VDD_3V3
- R54 pad 2: GND -> PSE_I2C_SCL
- R55 pad 1: VDD_3V3 -> T113_DZQ
- R55 pad 2: LED_PWR_A -> GND
- R56 pad 2: LED_STA_A -> SOC_RESET_N
- R6 pad 1: KSZ_ISET -> BOOST_FB
- R7 pad 1: KSZ_S_REXT -> BOOST_COMP
- R7 pad 2: GND -> BOOST_COMP_MID
- R8 pad 1: VDD_3V3 -> VIN_24V
- R8 pad 2: KSZ_RESET_N -> BOOST_PG
- R9 pad 1: VDD_3V3 -> COMP
- R9 pad 2: SPI_MOSI -> COMP_MID
- U13 pad 28: VIN_48V -> VBUS_48V
- U6 pad 2: VIN_48V -> VIN_24V
- U6 pad 3: VIN_48V -> VIN_24V
- U7 pad 10: (no net) -> SD_CMD
- U7 pad 11: (no net) -> SD_D3
- U7 pad 12: (no net) -> SD_D2
- U7 pad 28: N$11 -> N$12
- U7 pad 30: N$12 -> N$13
- U7 pad 43: (no net) -> LED_FAULT
- U7 pad 7: (no net) -> SD_D1
- U7 pad 8: (no net) -> SD_D0
- U7 pad 9: (no net) -> SD_CLK
- U9 pad 28: VIN_48V -> VBUS_48V
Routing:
- net SD_D3: track 0.00 -> 43.9 mm, vias 0 -> 1
- net P4_DN: track 0.00 -> 43.5 mm
- net SD_D0: track 0.00 -> 43.3 mm, vias 0 -> 1
- net SD_D2: track 0.00 -> 43.2 mm, vias 0 -> 1
- net SD_D1: track 0.00 -> 43.1 mm, vias 0 -> 1
- net SD_CLK: track 0.00 -> 43.0 mm, vias 0 -> 1
- net P5_AN: track 0.00 -> 43.0 mm
- net SD_CMD: track 0.00 -> 42.1 mm, vias 0 -> 1
- net P5_AP: track 0.00 -> 41.7 mm
- net P4_CN: track 0.00 -> 40.7 mm
- net P4_DP: track 0.00 -> 39.3 mm
- net P5_BP: track 0.00 -> 39.3 mm
- net P4_BN: track 0.00 -> 37.9 mm
- net P5_BN: track 0.00 -> 37.9 mm
- net P4_CP: track 0.00 -> 36.8 mm
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- added copper zone on In1.Cu, net GND
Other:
- board size 110 x 53 mm -> 130 x 80 mm
- copper layers 2 -> 4
